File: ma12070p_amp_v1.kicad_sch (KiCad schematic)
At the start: 81 parts, among them J2 Screw_Terminal_01x04, J3 Screw_Terminal_01x02, U1 MA12070P, U2 TPS62175DQC

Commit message: change
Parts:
- removed C10, C9: 1uF, Capacitor_THT:C_Rect_L13.0mm_W5.0mm_P10.00mm_FKS3_FKP3_MKS4, symbol Device:C
- removed C11, C7: 0.47uF, Capacitor_THT:C_Rect_L7.2mm_W4.5mm_P5.00mm_FKS2_FKP2_MKS2_MKP2, symbol Device:C
- removed COUTBUCK0: 22uF, Capacitor_THT:CP_Radial_D6.3mm_P2.50mm, symbol Device:CP
- removed CPVDD0B3: 1uF, Capacitor_SMD:C_1206_3216Metric, symbol Device:C
- removed JP1, JP2, JP3, JP4: Jumper_3_Open, Connector_PinHeader_2.54mm:PinHeader_1x03_P2.54mm_Vertical, symbol Jumper:Jumper_3_Open
- removed L4: 3.3uH, Inductor_SMD:L_Bourns_SRP1245A, symbol Device:L
- removed LBUCK0: SRN4026-100M, Inductor_SMD:L_Bourns-SRN4018, symbol Device:L
- removed R4: 3.6, Resistor_SMD:R_1206_3216Metric, symbol Device:R
- removed RB_FB1: 2M, Resistor_SMD:R_1206_3216Metric, symbol Device:R
- removed RB_FB2: 383k, Resistor_SMD:R_1206_3216Metric, symbol Device:R
- removed RB_PG0: 100k, Resistor_SMD:R_1206_3216Metric, symbol Device:R
- removed RCLK1, RENABLE1, RIN0B1, RIN1B1, RMUTE1: R, Resistor_SMD:R_1206_3216Metric, symbol Device:R
- removed U1: MA12070P, Package_DFN_QFN:QFN-64-1EP_9x9mm_P0.5mm_EP5.45x5.45mm, symbol Amplifier_Audio:MA12070P
- removed U2: TPS62175DQC, Package_SON:WSON-10-1EP_2x3mm_P0.5mm_EP0.84x2.4mm_ThermalVias, symbol Regulator_Switching:TPS62175DQC
- added C14, C16: 0.1uF, Capacitor_SMD:C_1206_3216Metric_Pad1.33x1.80mm_HandSolder, symbol Device:C
- added C15: 4,7uF, Capacitor_SMD:C_1206_3216Metric_Pad1.33x1.80mm_HandSolder, symbol Device:C
- added C19, C42: 1uF, Capacitor_SMD:C_1206_3216Metric_Pad1.33x1.80mm_HandSolder, symbol Device:C
- added C20: 22uF, Capacitor_SMD:C_1206_3216Metric_Pad1.33x1.80mm_HandSolder, symbol Device:C
- added C23, C27: 1uF, Capacitor_TH_TDK:C_Rect_L7.3_W4.5_P5.0, symbol Device:C
- added C24, C28: 0.47uF, Capacitor_TH_TDK:C_Rect_L7.3_W4.5_P5.0, symbol Device:C
- added JP1, JP3, JP5, JP9: SolderJumper_3_Open, Jumper:SolderJumper-3_P1.3mm_Open_Pad1.0x1.5mm, symbol Jumper:SolderJumper_3_Open
- added JP2, JP4, JP6, JP7, JP8: SolderJumper_2_Open, Jumper:SolderJumper-2_P1.3mm_Open_Pad1.0x1.5mm, symbol Jumper:SolderJumper_2_Open
- added L3: 10uH, Inductor_TH_Bourns:RLB0712-100KL, symbol Device:L
- added L6: 6.8uH, Inductor_TH_Bourns:L_Radia_Zylinder_D9.0_P5.0, symbol Device:L
- added R5, R7: 3.6, Resistor_SMD:R_1206_3216Metric_Pad1.30x1.75mm_HandSolder, symbol Device:R
- added U1: MAX16956AUBD/V+, max_16956:MAX16956AUBD&slash_V&plus_, symbol max_16956:MAX16956AUBD/V+
- added U2: MA12070P, Package_DFN_QFN:QFN-64-1EP_9x9mm_P0.5mm_EP5.45x5.45mm, symbol Amplifier_Audio:MA12070P
- C1: renamed from CSUP1; value 330uF/35V -> 100uF; DigikeyRef (none) -> UFG1V101MPM; infineonRef (none) -> CSUP1; property_1 (none) -> 35V; property_2 (none) -> UWT
- C10: renamed from CF0A0; footprint Capacitor_SMD:C_1206_3216Metric -> Capacitor_SMD:C_1206_3216Metric_Pad1.33x1.80mm_HandSolder; infineonRef (none) -> CF0A0; property_1 (none) -> X5R; property_2 (none) -> 25V
- C11: renamed from CF0A1; footprint Capacitor_SMD:C_1206_3216Metric -> Capacitor_SMD:C_1206_3216Metric_Pad1.33x1.80mm_HandSolder; infineonRef (none) -> CF0A1; property_1 (none) -> X5R; property_2 (none) -> 25V
- C12: renamed from C4; footprint Capacitor_THT:C_Rect_L13.0mm_W5.0mm_P10.00mm_FKS3_FKP3_MKS4 -> Capacitor_TH_TDK:C_Rect_L7.3_W4.5_P5.0; infineonRef (none) -> C0B0; property_1 (none) -> L13.0xW5.0
- C13: renamed from C5; footprint Capacitor_THT:C_Rect_L7.2mm_W4.5mm_P5.00mm_FKS2_FKP2_MKS2_MKP2 -> Capacitor_TH_TDK:C_Rect_L7.3_W4.5_P5.0; infineonRef (none) -> C0A1; property_1 (none) -> L7.2xW4.5
- C17: renamed from CF0B0; footprint Capacitor_SMD:C_1206_3216Metric -> Capacitor_SMD:C_1206_3216Metric_Pad1.33x1.80mm_HandSolder; infineonRef (none) -> CF0B0; property_1 (none) -> X5R; property_2 (none) -> 25V
- C18: renamed from CF0B1; footprint Capacitor_SMD:C_1206_3216Metric -> Capacitor_SMD:C_1206_3216Metric_Pad1.33x1.80mm_HandSolder; infineonRef (none) -> CF0B1; property_1 (none) -> X5R; property_2 (none) -> 25V
- C2: renamed from CSUP2; value 330uF/35V -> 100uF; DigikeyRef (none) -> UFG1V101MPM; infineonRef (none) -> CSUP2; property_1 (none) -> 35V; property_2 (none) -> UWT
- C21: renamed from CF1A0; footprint Capacitor_SMD:C_1206_3216Metric -> Capacitor_SMD:C_1206_3216Metric_Pad1.33x1.80mm_HandSolder; infineonRef (none) -> CF1A0; property_1 (none) -> X5R; property_2 (none) -> 25V
- C22: renamed from CF1A1; footprint Capacitor_SMD:C_1206_3216Metric -> Capacitor_SMD:C_1206_3216Metric_Pad1.33x1.80mm_HandSolder; infineonRef (none) -> CF1A1; property_1 (none) -> X5R; property_2 (none) -> 25V
- C25: renamed from CF1B0; footprint Capacitor_SMD:C_1206_3216Metric -> Capacitor_SMD:C_1206_3216Metric_Pad1.33x1.80mm_HandSolder; infineonRef (none) -> CF1B0; property_1 (none) -> X5R; property_2 (none) -> 25V
- C26: renamed from CF1B1; footprint Capacitor_SMD:C_1206_3216Metric -> Capacitor_SMD:C_1206_3216Metric_Pad1.33x1.80mm_HandSolder; infineonRef (none) -> CF1B1; property_1 (none) -> X5R; property_2 (none) -> 25V
- C29: renamed from CGD1; footprint Capacitor_SMD:C_1206_3216Metric -> Capacitor_SMD:C_1206_3216Metric_Pad1.33x1.80mm_HandSolder; infineonRef (none) -> CGD0; property_1 (none) -> X7R; property_2 (none) -> 25V
- C3: renamed from CPVDD0B0; footprint Capacitor_SMD:C_1206_3216Metric -> Capacitor_SMD:C_1206_3216Metric_Pad1.33x1.80mm_HandSolder; infineonRef (none) -> CPVDD0B; property_1 (none) -> X5R; property_2 (none) -> 50V
- C30: renamed from CGD1N1; footprint Capacitor_SMD:C_1206_3216Metric -> Capacitor_SMD:C_1206_3216Metric_Pad1.33x1.80mm_HandSolder; infineonRef (none) -> CGD1N1; property_1 (none) -> X5R; property_2 (none) -> 50V
- C31: renamed from CGD1N0; footprint Capacitor_SMD:C_1206_3216Metric -> Capacitor_SMD:C_1206_3216Metric_Pad1.33x1.80mm_HandSolder; infineonRef (none) -> CGD1N0; property_1 (none) -> X7R; property_2 (none) -> 50V
- C32: renamed from COUTBUCK1; value 1uF -> 22uF; footprint Capacitor_SMD:C_1206_3216Metric -> Capacitor_SMD:C_1206_3216Metric_Pad1.33x1.80mm_HandSolder; infineonRef (none) -> COUNTBUCK0; property_2 (none) -> 50V
- C33: renamed from COUTBUCK2; value 0.1uF -> 22uF; footprint Capacitor_SMD:C_1206_3216Metric -> Capacitor_SMD:C_1206_3216Metric_Pad1.33x1.80mm_HandSolder; infineonRef (none) -> COUNTBUCK1; property_2 (none) -> 50V
- C34: renamed from CFDC0; footprint Capacitor_SMD:C_1206_3216Metric -> Capacitor_SMD:C_1206_3216Metric_Pad1.33x1.80mm_HandSolder; infineonRef (none) -> CFDC; property_1 (none) -> X7R; property_2 (none) -> 25V
- C35: renamed from CGD0N1; footprint Capacitor_SMD:C_1206_3216Metric -> Capacitor_SMD:C_1206_3216Metric_Pad1.33x1.80mm_HandSolder; infineonRef (none) -> CGD0N1; property_1 (none) -> X5R; property_2 (none) -> 50V
- C36: renamed from CGD0N0; footprint Capacitor_SMD:C_1206_3216Metric -> Capacitor_SMD:C_1206_3216Metric_Pad1.33x1.80mm_HandSolder; infineonRef (none) -> CGD0N0; property_1 (none) -> X7R; property_2 (none) -> 50V
- C37: renamed from CVGDC0; footprint Capacitor_SMD:C_1206_3216Metric -> Capacitor_SMD:C_1206_3216Metric_Pad1.33x1.80mm_HandSolder; infineonRef (none) -> CVGDC; property_1 (none) -> X7R; property_2 (none) -> 25V
- C38: renamed from CGD0; footprint Capacitor_SMD:C_1206_3216Metric -> Capacitor_SMD:C_1206_3216Metric_Pad1.33x1.80mm_HandSolder; infineonRef (none) -> CGD1; property_1 (none) -> X7R; property_2 (none) -> 25V
- C39: renamed from CCDC0; footprint Capacitor_SMD:C_1206_3216Metric -> Capacitor_SMD:C_1206_3216Metric_Pad1.33x1.80mm_HandSolder; infineonRef (none) -> CCDC; property_1 (none) -> X7R; property_2 (none) -> 25V
- C4: renamed from CPVDD0A0; footprint Capacitor_SMD:C_1206_3216Metric -> Capacitor_SMD:C_1206_3216Metric_Pad1.33x1.80mm_HandSolder; infineonRef (none) -> CPVDD0A; property_1 (none) -> X7R; property_2 (none) -> 50V
- C40: renamed from CFGD0; footprint Capacitor_SMD:C_1206_3216Metric -> Capacitor_SMD:C_1206_3216Metric_Pad1.33x1.80mm_HandSolder; infineonRef (none) -> CFGD; property_1 (none) -> X7R; property_2 (none) -> 50V
- C41: renamed from CCREF0; footprint Capacitor_SMD:C_1206_3216Metric -> Capacitor_SMD:C_1206_3216Metric_Pad1.33x1.80mm_HandSolder; infineonRef (none) -> CCREF; property_1 (none) -> X7R; property_2 (none) -> 25V
- C43: renamed from CAPIN0B1; footprint Capacitor_SMD:C_1206_3216Metric -> Capacitor_SMD:C_1206_3216Metric_Pad1.33x1.80mm_HandSolder; infineonRef (none) -> CAPIN0B; property_1 (none) -> X5R; property_2 (none) -> 10V
- C44: renamed from CAPIN0A1; footprint Capacitor_SMD:C_1206_3216Metric -> Capacitor_SMD:C_1206_3216Metric_Pad1.33x1.80mm_HandSolder; infineonRef (none) -> CAPIN0A; property_1 (none) -> X5R; property_2 (none) -> 10V
- C45: renamed from CAPIN1B1; footprint Capacitor_SMD:C_1206_3216Metric -> Capacitor_SMD:C_1206_3216Metric_Pad1.33x1.80mm_HandSolder; infineonRef (none) -> CAPIN1B; property_1 (none) -> X5R; property_2 (none) -> 10V
- C46: renamed from CAPIN1A1; footprint Capacitor_SMD:C_1206_3216Metric -> Capacitor_SMD:C_1206_3216Metric_Pad1.33x1.80mm_HandSolder; infineonRef (none) -> CAPIN1A; property_1 (none) -> X5R; property_2 (none) -> 10V
- C5: renamed from CPVDD1A0; footprint Capacitor_SMD:C_1206_3216Metric -> Capacitor_SMD:C_1206_3216Metric_Pad1.33x1.80mm_HandSolder; infineonRef (none) -> CPVDD1A; property_1 (none) -> X7R; property_2 (none) -> 50V
- C6: renamed from CPVDD1B0; footprint Capacitor_SMD:C_1206_3216Metric -> Capacitor_SMD:C_1206_3216Metric_Pad1.33x1.80mm_HandSolder; infineonRef (none) -> CPVDD1B; property_1 (none) -> X5R; property_2 (none) -> 50V
- C7: renamed from CPVDD0B1; footprint Capacitor_SMD:C_1206_3216Metric -> Capacitor_SMD:C_1206_3216Metric_Pad1.33x1.80mm_HandSolder; infineonRef (none) -> CAVDD0; property_1 (none) -> X7R; property_2 (none) -> 25V
- C8: renamed from C3; footprint Capacitor_THT:C_Rect_L13.0mm_W5.0mm_P10.00mm_FKS3_FKP3_MKS4 -> Capacitor_TH_TDK:C_Rect_L7.3_W4.5_P5.0; infineonRef (none) -> C0A0; property_1 (none) -> L13.0xW5.0
- C9: renamed from C1; footprint Capacitor_THT:C_Rect_L7.2mm_W4.5mm_P5.00mm_FKS2_FKP2_MKS2_MKP2 -> Capacitor_TH_TDK:C_Rect_L7.3_W4.5_P5.0; infineonRef (none) -> C0B1; property_1 (none) -> L7.2xW4.5
- CIN1: renamed from CIN0; value 22nF -> 0.022uF; footprint Capacitor_SMD:C_1206_3216Metric -> Capacitor_SMD:C_1206_3216Metric_Pad1.33x1.80mm_HandSolder; infineonRef (none) -> CIN0; property_1 (none) -> X7R; property_2 (none) -> 50V
- CIN2: renamed from CIN1; value 22nF -> 0.022uF; footprint Capacitor_SMD:C_1206_3216Metric -> Capacitor_SMD:C_1206_3216Metric_Pad1.33x1.80mm_HandSolder; infineonRef (none) -> CIN1; property_1 (none) -> X7R; property_2 (none) -> 50V
- CONN3: renamed from PCTRL1; infineonRef (none) -> PCTRL1
- CONN4: renamed from PAUDIO1; infineonRef (none) -> PAUDIO1
- L1: renamed from LSUP0; value Ferrite 2743019447 -> 47; infineonRef (none) -> LSUP1
- L2, L5: value 3.3uH -> 6.8uH; footprint Inductor_SMD:L_Bourns_SRP1245A -> Inductor_TH_Bourns:L_Radia_Zylinder_D9.0_P5.0
- L4: renamed from L3; value 3.3uH -> 6.8uH; footprint Inductor_SMD:L_Bourns_SRP1245A -> Inductor_TH_Bourns:L_Radia_Zylinder_D9.0_P5.0
- LED1: renamed from CLIP_LED_0; footprint LED_SMD:LED_1206_3216Metric -> LED_SMD:LED_1206_3216Metric_Pad1.42x1.75mm_HandSolder; infineonRef (none) -> CLIP_LED_1
- LED2: renamed from ERROR_LED_0; footprint LED_SMD:LED_1206_3216Metric -> LED_SMD:LED_1206_3216Metric_Pad1.42x1.75mm_HandSolder; infineonRef (none) -> ERROR_LED_1
- R1: renamed from RPVDD1; footprint Resistor_SMD:R_1206_3216Metric -> Resistor_SMD:R_1206_3216Metric_Pad1.30x1.75mm_HandSolder; infineonRef (none) -> RPVDD1
- R2: renamed from R1; footprint Resistor_SMD:R_1206_3216Metric -> Resistor_SMD:R_1206_3216Metric_Pad1.30x1.75mm_HandSolder
- R3: value 3.6 -> 4.7k; footprint Resistor_SMD:R_1206_3216Metric -> Resistor_SMD:R_1206_3216Metric_Pad1.30x1.75mm_HandSolder
- R4: renamed from R2; footprint Resistor_SMD:R_1206_3216Metric -> Resistor_SMD:R_1206_3216Metric_Pad1.30x1.75mm_HandSolder
- R6: renamed from RCLIP_LED_0; footprint Resistor_SMD:R_1206_3216Metric -> Resistor_SMD:R_1206_3216Metric_Pad1.30x1.75mm_HandSolder; infineonRef (none) -> R_CLIP
- R8: renamed from RCLIP_ERROR_0; footprint Resistor_SMD:R_1206_3216Metric -> Resistor_SMD:R_1206_3216Metric_Pad1.30x1.75mm_HandSolder; infineonRef (none) -> R_ERROR
- renumbered J3 to CONN1, J2 to CONN2
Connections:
- net AD0: now also JP5.2 (C), U2.28 (AD0)
- net AD1: now also JP9.2 (C), U2.29 (AD1)
- net CLIP: now also U2.15 (~{CLIP})
- net ENABLE: now also JP2.2 (B), U2.33 (~{ENABLE})
- net GND: now also C8.2, C15.2, C16.2, C19.2, C20.2, C23.2, C24.1, C27.2, C28.2, JP2.1 (A), JP3.1 (A), JP5.1 (A), JP6.1 (A), JP7.1 (A), JP9.1 (A), U1.4 (PGND), U1.5 (AGND), U1.EPAD (EP), U2.1 (PVSS), U2.13 (PVSS), U2.14 (PVSS), U2.19 (AVSS), U2.2 (PVSS), U2.25 (AVSS), U2.26 (DVSS), U2.35 (PVSS), U2.36 (PVSS), U2.47 (PVSS), U2.48 (PVSS), U2.50 (MSEL1), U2.59 (DVSS); no longer C8.1
- net MUTE: now also JP4.2 (B), U2.34 (~{MUTE})
- net OUT0A: now also U2.4 (OUT0A), U2.5 (OUT0A)
- net OUT0B: now also U2.10 (OUT0B), U2.11 (OUT0B)
- net OUT1A: now also L5.2, U2.44 (OUT1A), U2.45 (OUT1A)
- net OUT1B: now also L6.2, U2.38 (OUT1B), U2.39 (OUT1B); no longer L5.2
- net PVDD: now also C15.1, C16.1, U1.10 (EN), U1.2 (SUP), U2.41 (PVDD), U2.42 (PVDD), U2.7 (PVDD), U2.8 (PVDD)
- net SDA: now also U2.30 (SDA)
- net SDL: now also U2.27 (SCL)
- net VDD: now also R3.1, JP1.2 (C), JP3.3 (B), JP4.1 (A), JP5.3 (B), JP9.3 (B), U2.17 (AVDD), U2.51 (MSEL0), U2.55 (DVDD)
- net at CONN2.2 (Pin_2): now also C13.1, L4.1, R4.2; no longer R3.1
- net at R3.2: now also U1.6 (*RESET)
- net at CONN2.1 (Pin_1): now also C9.2, L2.1, R2.1; no longer L5.1
- net at R2.2: now also C8.1; no longer C8.2
- net at C17.2, C18.2: now also U2.12 (CF0BN)
- net at C41.1: now also U2.20 (CREF)
- net at C10.2, C11.2: now also U2.3 (CF0AN)
- net at C25.2, C26.2: now also U2.37 (CF1BN)
- net at C25.1, C26.1: now also U2.40 (CF1BP)
- net at C21.1, C22.1: now also U2.43 (CF1AP)
- net at C21.2, C22.2: now also U2.46 (CF1AN)
- net at C29.1, C30.1, C31.2: now also U2.52 (CGD1N)
- net at C29.2: now also U2.53 (CGD1P)
- net at C37.1: now also U2.54 (VGDC)
- net at C39.1: now also U2.56 (CDC)
- net at C34.1: now also U2.57 (CFDCP)
- net at C34.2: now also U2.58 (CFDCN)
- net at C10.1, C11.1: now also U2.6 (CF0AP)
- net at C35.1, C36.2, C38.1: now also U2.60 (CGD0P)
- net at C38.2: now also U2.61 (CGD0N)
- net at C40.2: now also U2.62 (CFGDP)
- net at C40.1: now also U2.63 (CFGDN)
- net at C17.1, C18.1: now also U2.9 (CF0BP)
- net at C44.1, CONN4.2 (Pin_2): now also JP6.2 (B)
- net at C45.1, CONN4.5 (Pin_5): now also JP7.2 (B), JP8.2 (B)
- net ERROR renamed ERR
- net ERR: now also U2.16 (~{ERROR})
- net SCLK renamed IN0A
- net IN0A: now also U2.21 (IN0A)
- net SD0 renamed IN1A
- net IN1A: now also U2.23 (IN1A)
- net SD1 renamed IN1B
- net IN1B: now also U2.24 (IN1B)
- net WS renamed IN0B
- net IN0B: now also U2.22 (IN0B)
- new net: C24.2, CONN2.3 (Pin_3), L5.1, R5.1
- new net: C28.1, CONN2.4 (Pin_4), L6.1, R7.2
- new net: C19.1, U1.7 (MODE), U1.8 (BIAS)
- new net: C14.2, L3.1, U1.3 (LX)
- new net: C14.1, U1.1 (BST)
- new net: C27.1, R7.1
- new net: C23.1, R5.2
- new net Buck_5V: JP1.1 (A)
- new net CLKIO: JP8.1 (A), U2.32 (CLKIO)
- new net CLKMS: JP3.2 (C), U2.31 (CLKMS)
- new net IC_5V: C20.1, JP1.3 (B), L3.2, U1.9 (OUT)
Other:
- moved on the sheet: C12, C13, C3, C32, C33, C34, C4, C5, C6, C7, C8, C9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

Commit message: V0.1
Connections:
- net GND: now also C42.2
- net VDD: now also C42.1
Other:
- moved on the sheet: C42
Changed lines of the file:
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@@
     (pin "EPAD")
+  )
+  (symbol (lib_id "power:VDD") (at 205.105 80.01 0) (unit 1)
+    (in_bom yes) (on_board yes)
+    (property "Reference" "#PWR0102" (id 0) (at 205.105 83.82 0)
+      (effects (font (size 1.27 1.27)) hide)
+    )
+    (property "Value" "VDD" (id 1) (at 205.105 76.2 0))
+    (property "Footprint" "" (id 2) (at 205.105 80.01 0)
+      (effects (font (size 1.27 1.27)) hide)
+    )
+    (property "Datasheet" "" (id 3) (at 205.105 80.01 0)
+      (effects (font (size 1.27 1.27)) hide)
+    )
+    (pin "1")
   )
   (symbol (lib_id "Mechanical:MountingHole_Pad") (at 254.635 147.32 270) (unit 1)
@@
     (pin "2")
   )
-  (symbol (lib_id "Device:C") (at 181.61 140.97 0) (unit 1)
+  (symbol (lib_id "Device:C") (at 205.105 83.82 0) (unit 1)
     (in_bom yes) (on_board yes) (fields_autoplaced)
-    (property "Reference" "C42" (id 0) (at 185.42 139.6999 0)
-      (effects (font (size 1.27 1.27)) (justify left))
-    )
-    (property "Value" "1uF" (id 1) (at 185.42 142.2399 0)
-      (effects (font (size 1.27 1.27)) (justify left))
-    )
-    (property "Footprint" "Capacitor_SMD:C_1206_3216Metric_Pad1.33x1.80mm_HandSolder" (id 2) (at 182.5752 144.78 0)
-      (effects (font (size 1.27 1.27)) hide)
-    )
-    (property "Datasheet" "~" (id 3) (at 181.61 140.97 0)
-      (effects (font (size 1.27 1.27)) hide)
-    )
-    (property "infineonRef" "DVDD0" (id 4) (at 181.61 140.97 0)
-      (effects (font (size 1.27 1.27)) hide)
-    )
-    (property "property_1" "X7R" (id 5) (at 181.61 140.97 0)
-      (effects (font (size 1.27 1.27)) hide)
-    )
-    (property "property_2" "25V" (id 6) (at 181.61 140.97 0)
-      (effects (font (size 1.27 1.27)) hide)
-    )
-    (pin "1")
-    (pin "2")
+    (property "Reference" "C42" (id 0) (at 208.915 82.5499 0)
+      (effects (font (size 1.27 1.27)) (justify left))
+    )
+    (property "Value" "1uF" (id 1) (at 208.915 85.0899 0)
+      (effects (font (size 1.27 1.27)) (justify left))
+    )
+    (property "Footprint" "Capacitor_SMD:C_1206_3216Metric_Pad1.33x1.80mm_HandSolder" (id 2) (at 206.0702 87.63 0)
+      (effects (font (size 1.27 1.27)) hide)
+    )
+    (property "Datasheet" "~" (id 3) (at 205.105 83.82 0)
+      (effects (font (size 1.27 1.27)) hide)
+    )
+    (property "infineonRef" "DVDD0" (id 4) (at 205.105 83.82 0)
+      (effects (font (size 1.27 1.27)) hide)
+    )
+    (property "property_1" "X7R" (id 5) (at 205.105 83.82 0)
+      (effects (font (size 1.27 1.27)) hide)
+    )
+    (property "property_2" "25V" (id 6) (at 205.105 83.82 0)
+      (effects (font (size 1.27 1.27)) hide)
+    )
+    (pin "1")
+    (pin "2")
+  )
+  (symbol (lib_id "power:GND") (at 205.105 87.63 0) (unit 1)
+    (in_bom yes) (on_board yes)
+    (property "Reference" "#PWR0101" (id 0) (at 205.105 93.98 0)
+      (effects (font (size 1.27 1.27)) hide)
+    )
+    (property "Value" "GND" (id 1) (at 205.232 92.0242 0))
+    (property "Footprint" "" (id 2) (at 205.105 87.63 0)
+      (effects (font (size 1.27 1.27)) hide)
+    )
+    (property "Datasheet" "" (id 3) (at 205.105 87.63 0)
+      (effects (font (size 1.27 1.27)) hide)
+    )
+    (pin "1")
   )
   (symbol (lib_id "Device:C") (at 69.215 153.67 180) (unit 1)
@@
       (reference "#PWR037") (unit 1) (value "GND") (footprint "")
     )
+    (path "/f21a8e94-56fc-42a7-bf10-985e4c816b97"
+      (reference "#PWR0101") (unit 1) (value "GND") (footprint "")
+    )
+    (path "/c3d9cac1-8822-4065-b002-b032d4a0595a"
+      (reference "#PWR0102") (unit 1) (value "VDD") (footprint "")
+    )
     (path "/00000000-0000-0000-0000-0000606e0996"

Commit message: finished DRC
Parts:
- C1, C2: symbol Device:CP -> Device:C
- R1: footprint Resistor_SMD:R_1206_3216Metric_Pad1.30x1.75mm_HandSolder -> Resistor_SMD:R_2512_6332Metric_Pad1.40x3.35mm_HandSolder
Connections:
- net Buck_5V renamed Ext_supply_5V

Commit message: updated some components
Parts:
- C10, C11, C17, C18, C21, C22, C25, C26: manufacturerRef (none) -> GRM31CR71E106KA12L
- C14, C16: manufacturerRef (none) -> GRM31C5C1H104JA01K; property_1 (none) -> C0G/NP0; property_2 (none) -> 50V
- C19: manufacturerRef (none) -> GCJ31MR71H105KA12L; property_1 (none) -> X7R; property_2 (none) -> 50V
- C29, C34, C37, C38, C39, C41, C42, C7: manufacturerRef (none) -> GCJ31MR71H105KA12L; property_2 25V -> 50V
- C3, C30, C35, C6: manufacturerRef (none) -> GCJ31MR71H105KA12L; property_1 X5R -> X7R
- C31, C36, C4, C40, C5: manufacturerRef (none) -> GRM31C5C1H104JA01K; property_1 X7R -> C0G/NP0
- C32, C33: value 22uF -> 10uF
- C43, C44, C45, C46: manufacturerRef (none) -> GCJ31MR71H105KA12L; property_1 X5R -> X7R; property_2 10V -> 50V
- CIN1, CIN2: manufacturerRef (none) -> GRM3195C1H223JA01D; property_1 X7R -> C0G/NP0
- L2, L4, L5, L6: manufacturerRef (none) -> RLB9012-6R8ML; property_1 (none) -> D9.0xH12.2
- L3: manufacturerRef (none) -> RLB0712-100KL; property_1 (none) -> D6.7xH

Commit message: changed output filter inductors
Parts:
- L2, L4, L5, L6: footprint Inductor_TH_Bourns:L_Radia_Zylinder_D9.0_P5.0 -> Inductor_Murata_TH:L_Radial_TH_Murata_D16.9_P14.0
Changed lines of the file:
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@@
     (property "Reference" "L2" (id 0) (at 231.14 29.21 90))
     (property "Value" "6.8uH" (id 1) (at 233.045 31.115 90))
-    (property "Footprint" "Inductor_TH_Bourns:L_Radia_Zylinder_D9.0_P5.0" (id 2) (at 233.68 33.02 0)
+    (property "Footprint" "Inductor_Murata_TH:L_Radial_TH_Murata_D16.9_P14.0" (id 2) (at 233.68 33.02 0)
       (effects (font (size 1.27 1.27)) hide)
     )
@@
     (property "Reference" "L4" (id 0) (at 233.68 64.77 90))
     (property "Value" "6.8uH" (id 1) (at 234.315 66.675 90))
-    (property "Footprint" "Inductor_TH_Bourns:L_Radia_Zylinder_D9.0_P5.0" (id 2) (at 234.315 68.58 0)
+    (property "Footprint" "Inductor_Murata_TH:L_Radial_TH_Murata_D16.9_P14.0" (id 2) (at 234.315 68.58 0)
       (effects (font (size 1.27 1.27)) hide)
     )
@@
     (property "Reference" "L5" (id 0) (at 233.68 74.295 90))
     (property "Value" "6.8uH" (id 1) (at 233.68 75.565 90))
-    (property "Footprint" "Inductor_TH_Bourns:L_Radia_Zylinder_D9.0_P5.0" (id 2) (at 234.315 73.025 0)
+    (property "Footprint" "Inductor_Murata_TH:L_Radial_TH_Murata_D16.9_P14.0" (id 2) (at 234.315 73.025 0)
       (effects (font (size 1.27 1.27)) hide)
     )
@@
     (property "Reference" "L6" (id 0) (at 232.41 111.76 90))
     (property "Value" "6.8uH" (id 1) (at 234.315 109.855 90))
-    (property "Footprint" "Inductor_TH_Bourns:L_Radia_Zylinder_D9.0_P5.0" (id 2) (at 234.315 108.585 0)
+    (property "Footprint" "Inductor_Murata_TH:L_Radial_TH_Murata_D16.9_P14.0" (id 2) (at 234.315 108.585 0)
       (effects (font (size 1.27 1.27)) hide)
     )
@@
     )
     (path "/00000000-0000-0000-0000-00005fb207fb"
-      (reference "L2") (unit 1) (value "6.8uH") (footprint "Inductor_TH_Bourns:L_Radia_Zylinder_D9.0_P5.0")
+      (reference "L2") (unit 1) (value "6.8uH") (footprint "Inductor_Murata_TH:L_Radial_TH_Murata_D16.9_P14.0")
     )
     (path "/33c69e16-af93-41aa-bbd1-55b41472b999"
@@
     )
     (path "/00000000-0000-0000-0000-00005fb22f2b"
-      (reference "L4") (unit 1) (value "6.8uH") (footprint "Inductor_TH_Bourns:L_Radia_Zylinder_D9.0_P5.0")
+      (reference "L4") (unit 1) (value "6.8uH") (footprint "Inductor_Murata_TH:L_Radial_TH_Murata_D16.9_P14.0")
     )
     (path "/23f2b863-9d6b-443c-80f8-be18f651806a"
-      (reference "L5") (unit 1) (value "6.8uH") (footprint "Inductor_TH_Bourns:L_Radia_Zylinder_D9.0_P5.0")
+      (reference "L5") (unit 1) (value "6.8uH") (footprint "Inductor_Murata_TH:L_Radial_TH_Murata_D16.9_P14.0")
     )
     (path "/d8a5ee5e-ae92-4ba0-acee-93649e3b6139"
-      (reference "L6") (unit 1) (value "6.8uH") (footprint "Inductor_TH_Bourns:L_Radia_Zylinder_D9.0_P5.0")
+      (reference "L6") (unit 1) (value "6.8uH") (footprint "Inductor_Murata_TH:L_Radial_TH_Murata_D16.9_P14.0")
     )
     (path "/00000000-0000-0000-0000-000060423aa3"

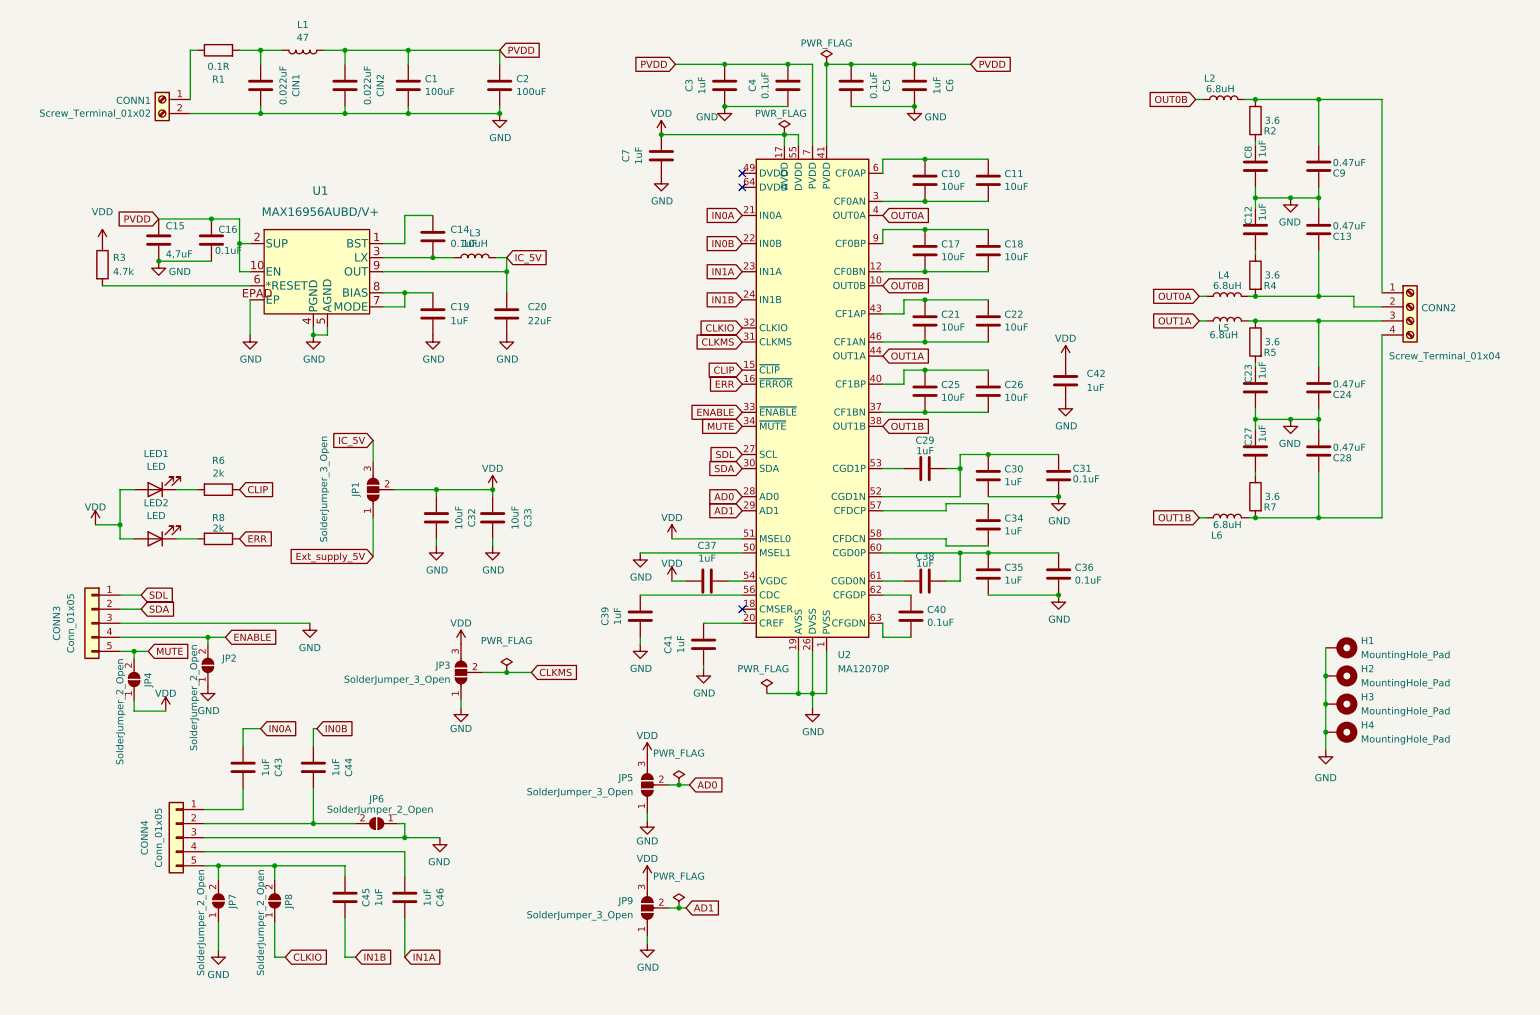
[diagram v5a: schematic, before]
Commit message: made d3 Models for inductors
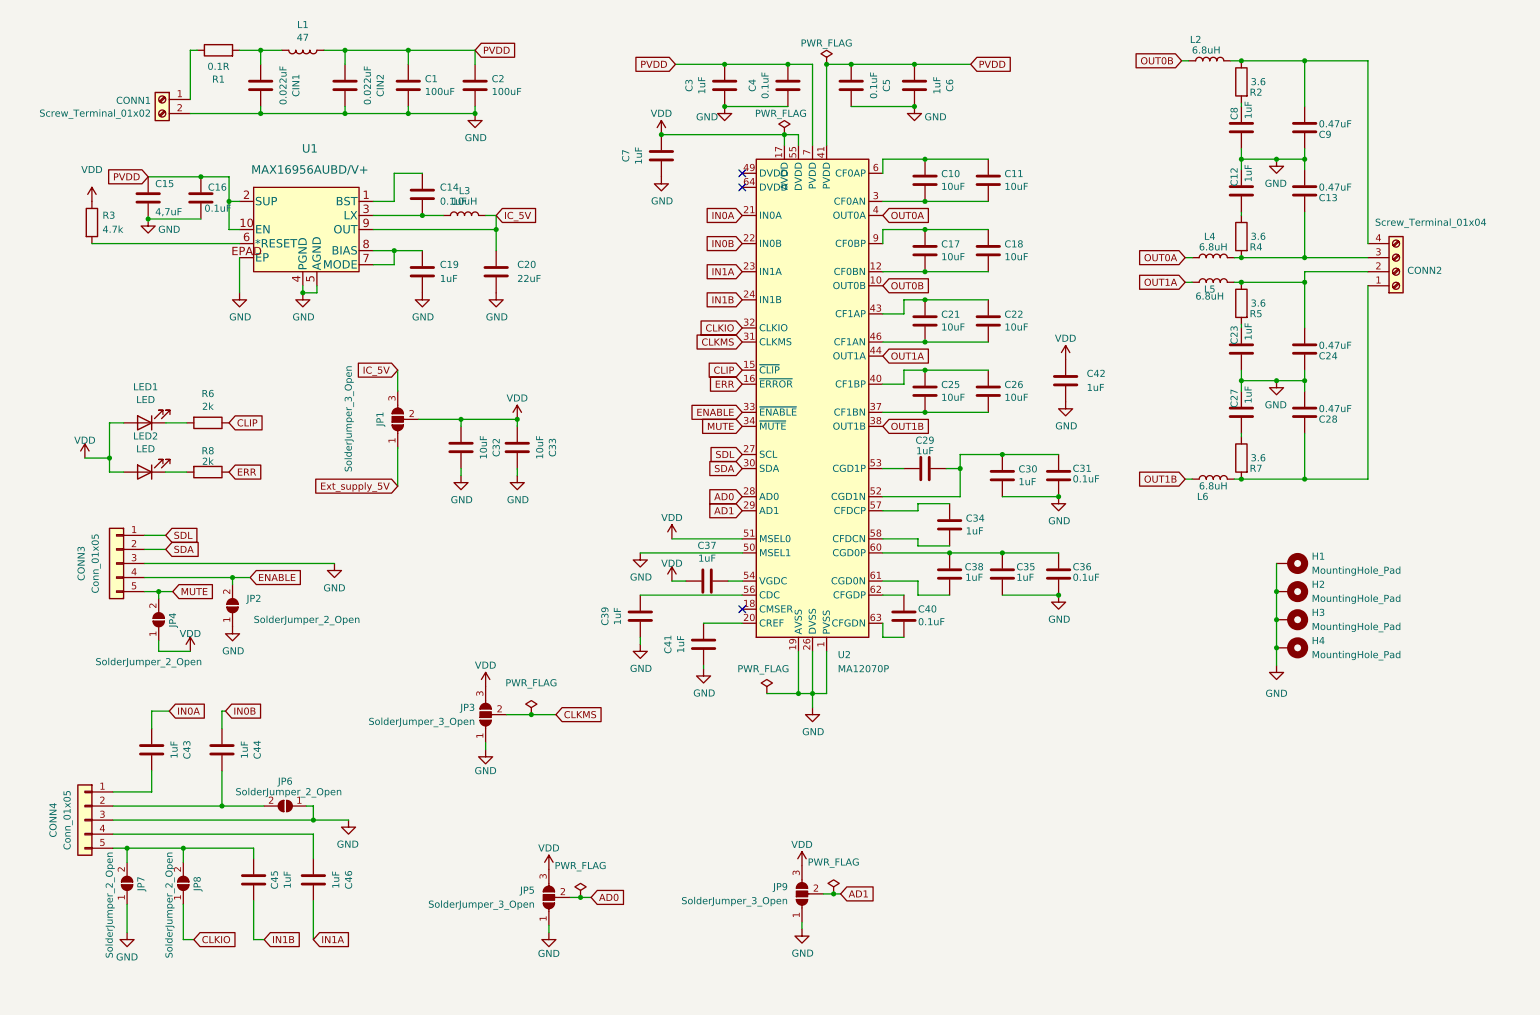
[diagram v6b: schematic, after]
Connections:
- net at C9.2, L2.1, R2.1: now also CONN2.4 (Pin_4); no longer CONN2.1 (Pin_1)
- net at C13.1, L4.1, R4.2: now also CONN2.3 (Pin_3); no longer CONN2.2 (Pin_2)
- net at C24.2, L5.1, R5.1: now also CONN2.2 (Pin_2); no longer CONN2.3 (Pin_3)
- net at C28.1, L6.1, R7.2: now also CONN2.1 (Pin_1); no longer CONN2.4 (Pin_4)
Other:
- moved on the sheet: C12, C13, C14, C15, C16, C19, C2, C20, C23, C24, C27, C28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
